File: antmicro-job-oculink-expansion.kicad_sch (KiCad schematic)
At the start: 104 parts, among them J1 OCuLink_x4_Amphenol_G14A42121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, J2 Plug_Samtec_ERM8_2x40_ERM8-04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, U1 MAX3373EEKA+, U2 PI3EQX16904GL, U3 PI3EQX16904GL

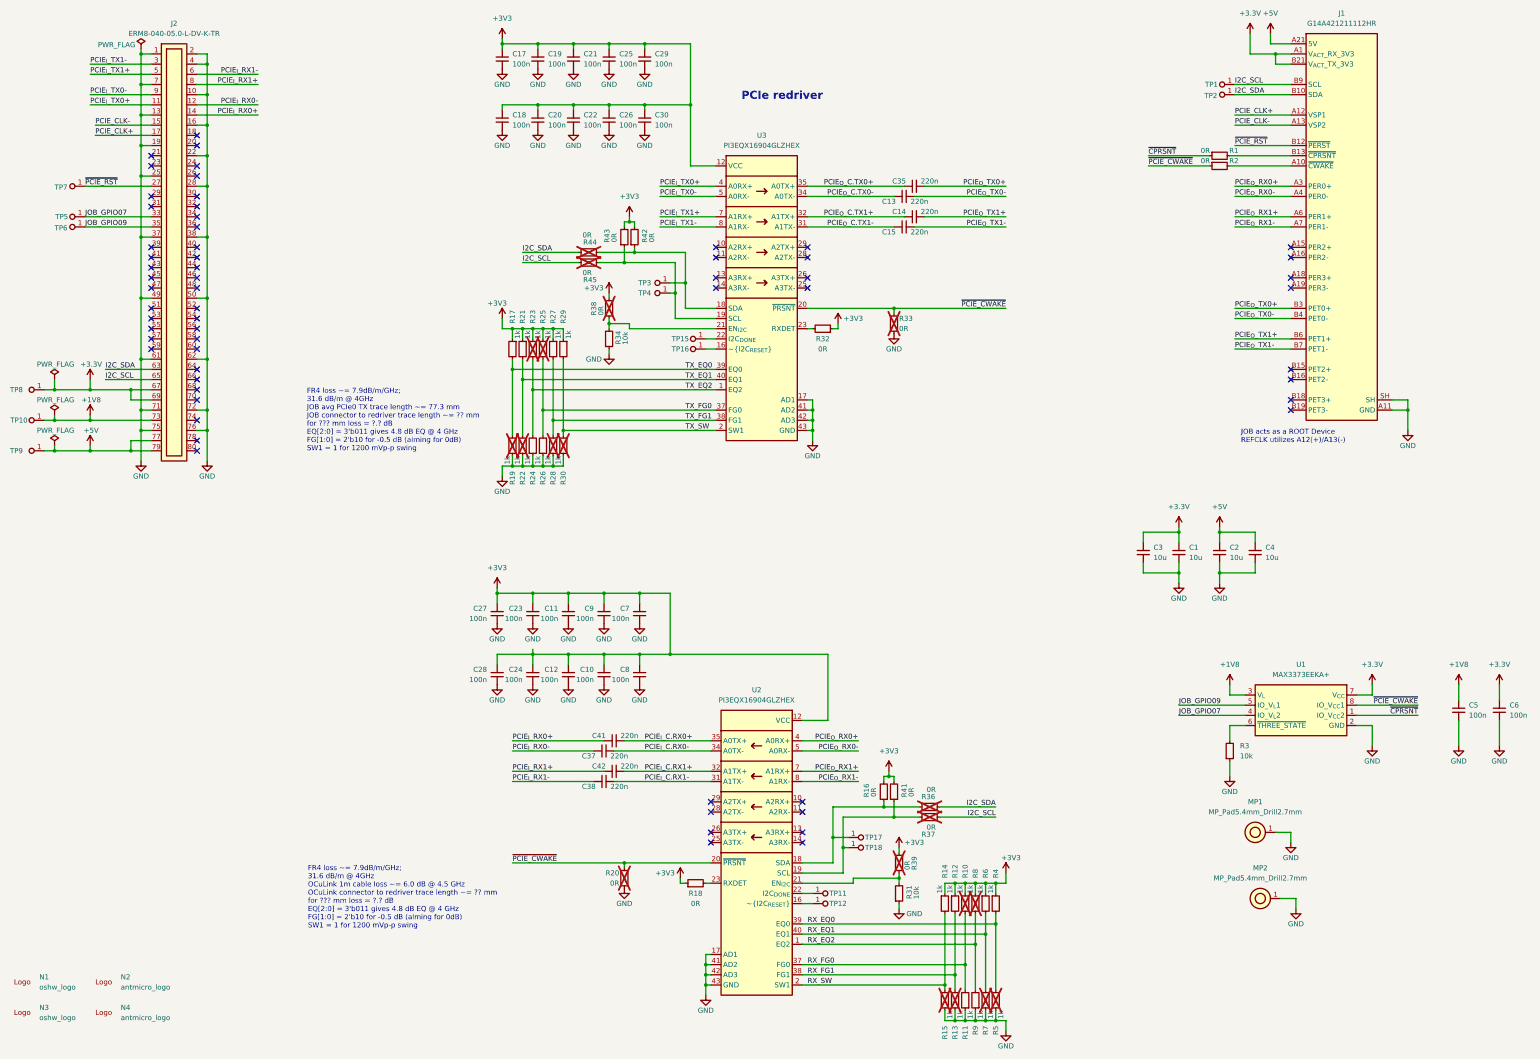
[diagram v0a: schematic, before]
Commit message: [#76297] Rename +3.3V to +3V3
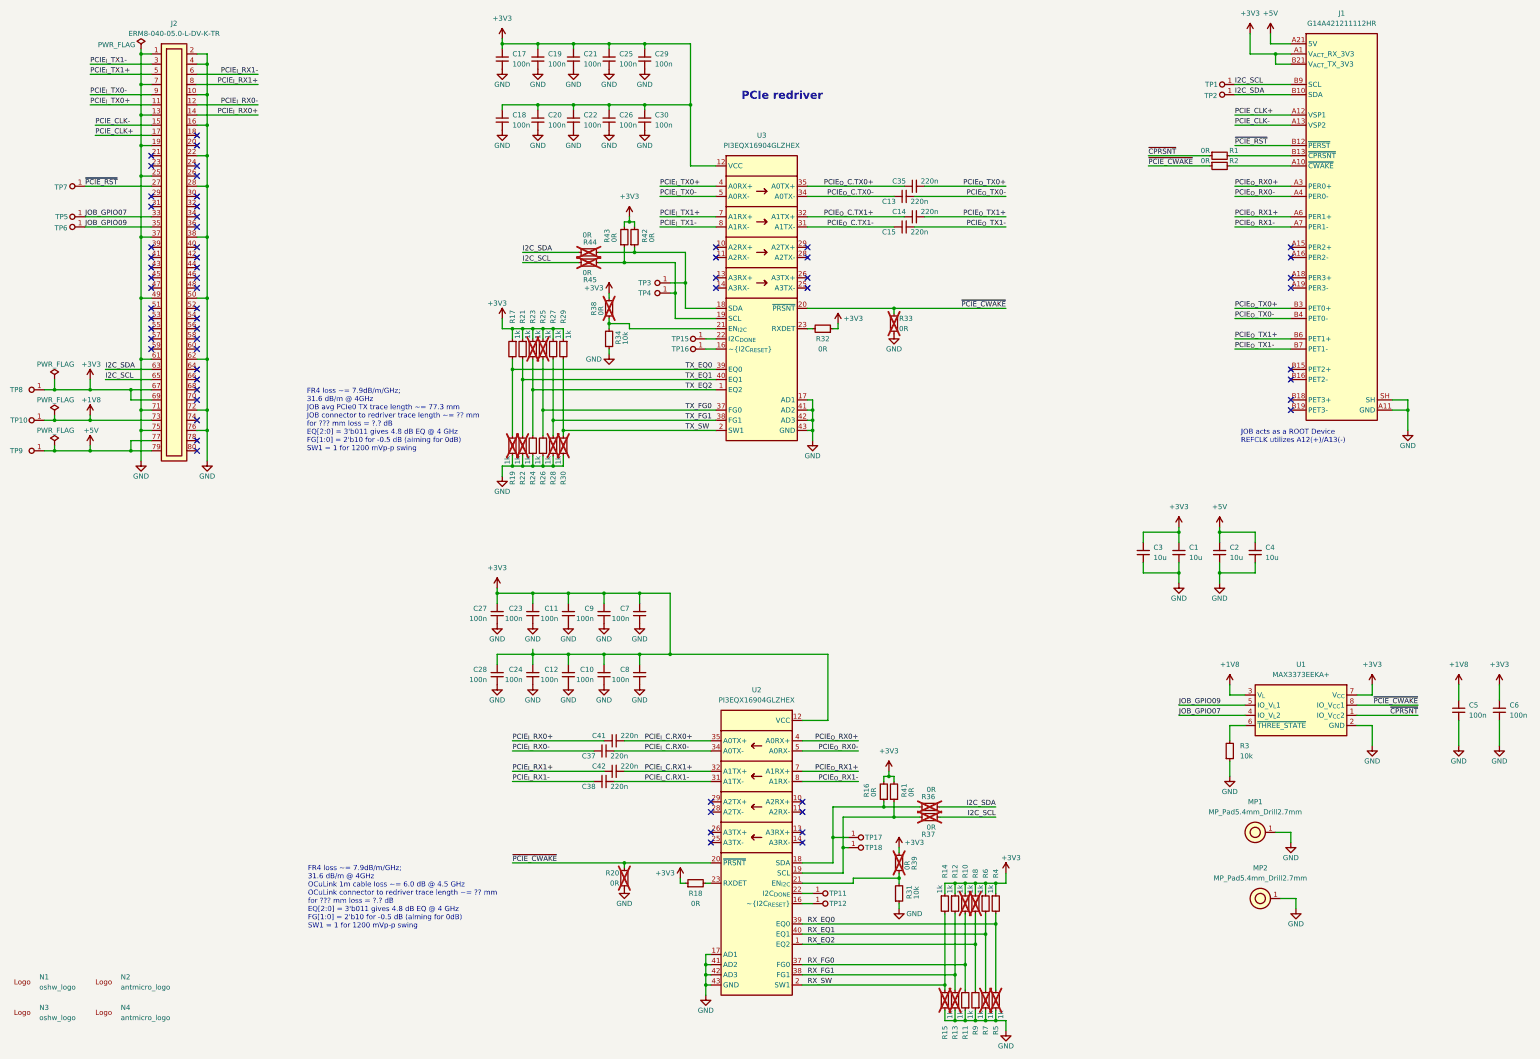
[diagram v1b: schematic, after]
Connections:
- net +3.3V is gone; now on net +3V3: C1.2, C3.2, C6.2, J1.A1 (V_{ACT}_RX_3V3), J1.B21 (V_{ACT}_TX_3V3), J2.67, J2.69, TP8.1, U1.7 (V_{CC})
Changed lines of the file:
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@@
 			)
 		)
-		(property "Value" "+3.3V"
+		(property "Value" "+3V3"
 			(at 396.24 182.88 0)
 			(effects
@@
 			)
 		)
-		(property "Value" "+3.3V"
+		(property "Value" "+3V3"
 			(at 316.23 143.51 0)
 			(effects
@@
 			)
 		)
-		(property "Value" "+3.3V"
+		(property "Value" "+3V3"
 			(at 44.704 107.95 0)
 			(effects
@@
 			)
 		)
-		(property "Value" "+3.3V"
+		(property "Value" "+3V3"
 			(at 334.01 20.32 0)
 			(effects
@@
 			)
 		)
-		(property "Value" "+3.3V"
+		(property "Value" "+3V3"
 			(at 364.49 182.88 0)
 			(effects

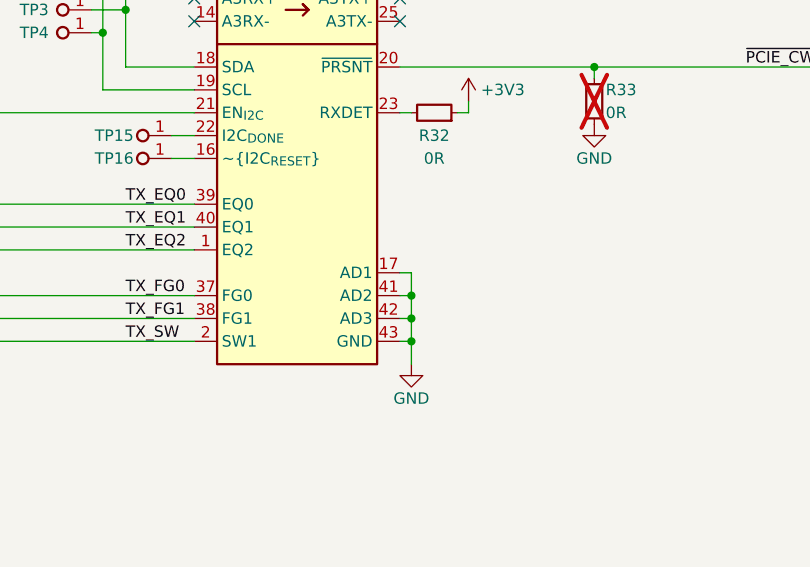
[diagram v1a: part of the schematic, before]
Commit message: [#76297] Fix same redriver I2C addresses
U1 is now accessible on I2C address 0x70 and U2 is accessible on address
0x72.
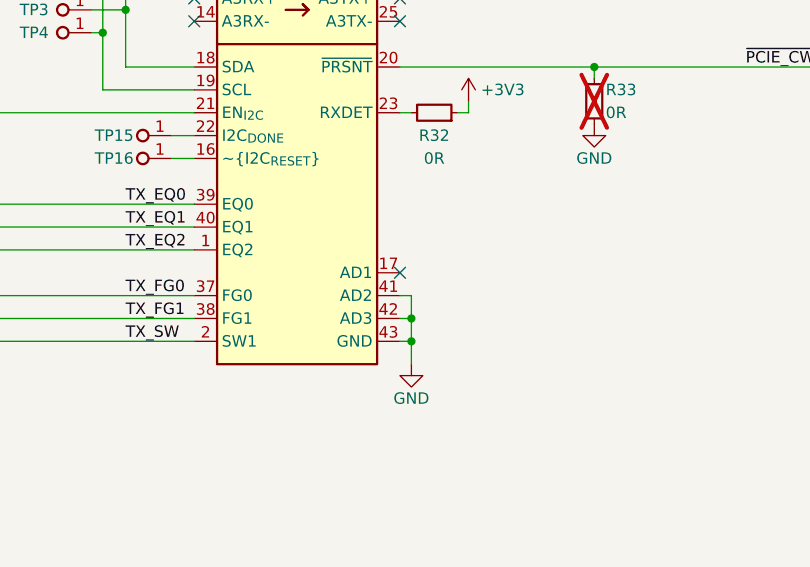
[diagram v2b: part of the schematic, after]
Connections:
- net GND: no longer U3.17 (AD1)
- no-connect marks 63 -> 64
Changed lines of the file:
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@@
-	)
-	(junction
-		(at 224.79 119.38)
-		(diameter 0)
-		(color 0 0 0 0)
 	)
 	(junction
@@
 	)
 	(no_connect
+		(at 223.52 116.84)
+	)
+	(no_connect
 		(at 71.12 104.14)
 	)
@@
 	(wire
 		(pts
-			(xy 224.79 116.84) (xy 224.79 119.38)
-		)
-		(stroke
-			(width 0)
-			(type default)
-		)
-	)
-	(wire
-		(pts
 			(xy 260.35 269.24) (xy 260.35 271.78)
 		)
@@
 		)
 		(stroke
-			(width 0)
-			(type default)
-		)
-	)
-	(wire
-		(pts
-			(xy 223.52 116.84) (xy 224.79 116.84)
-		)
-		(stroke

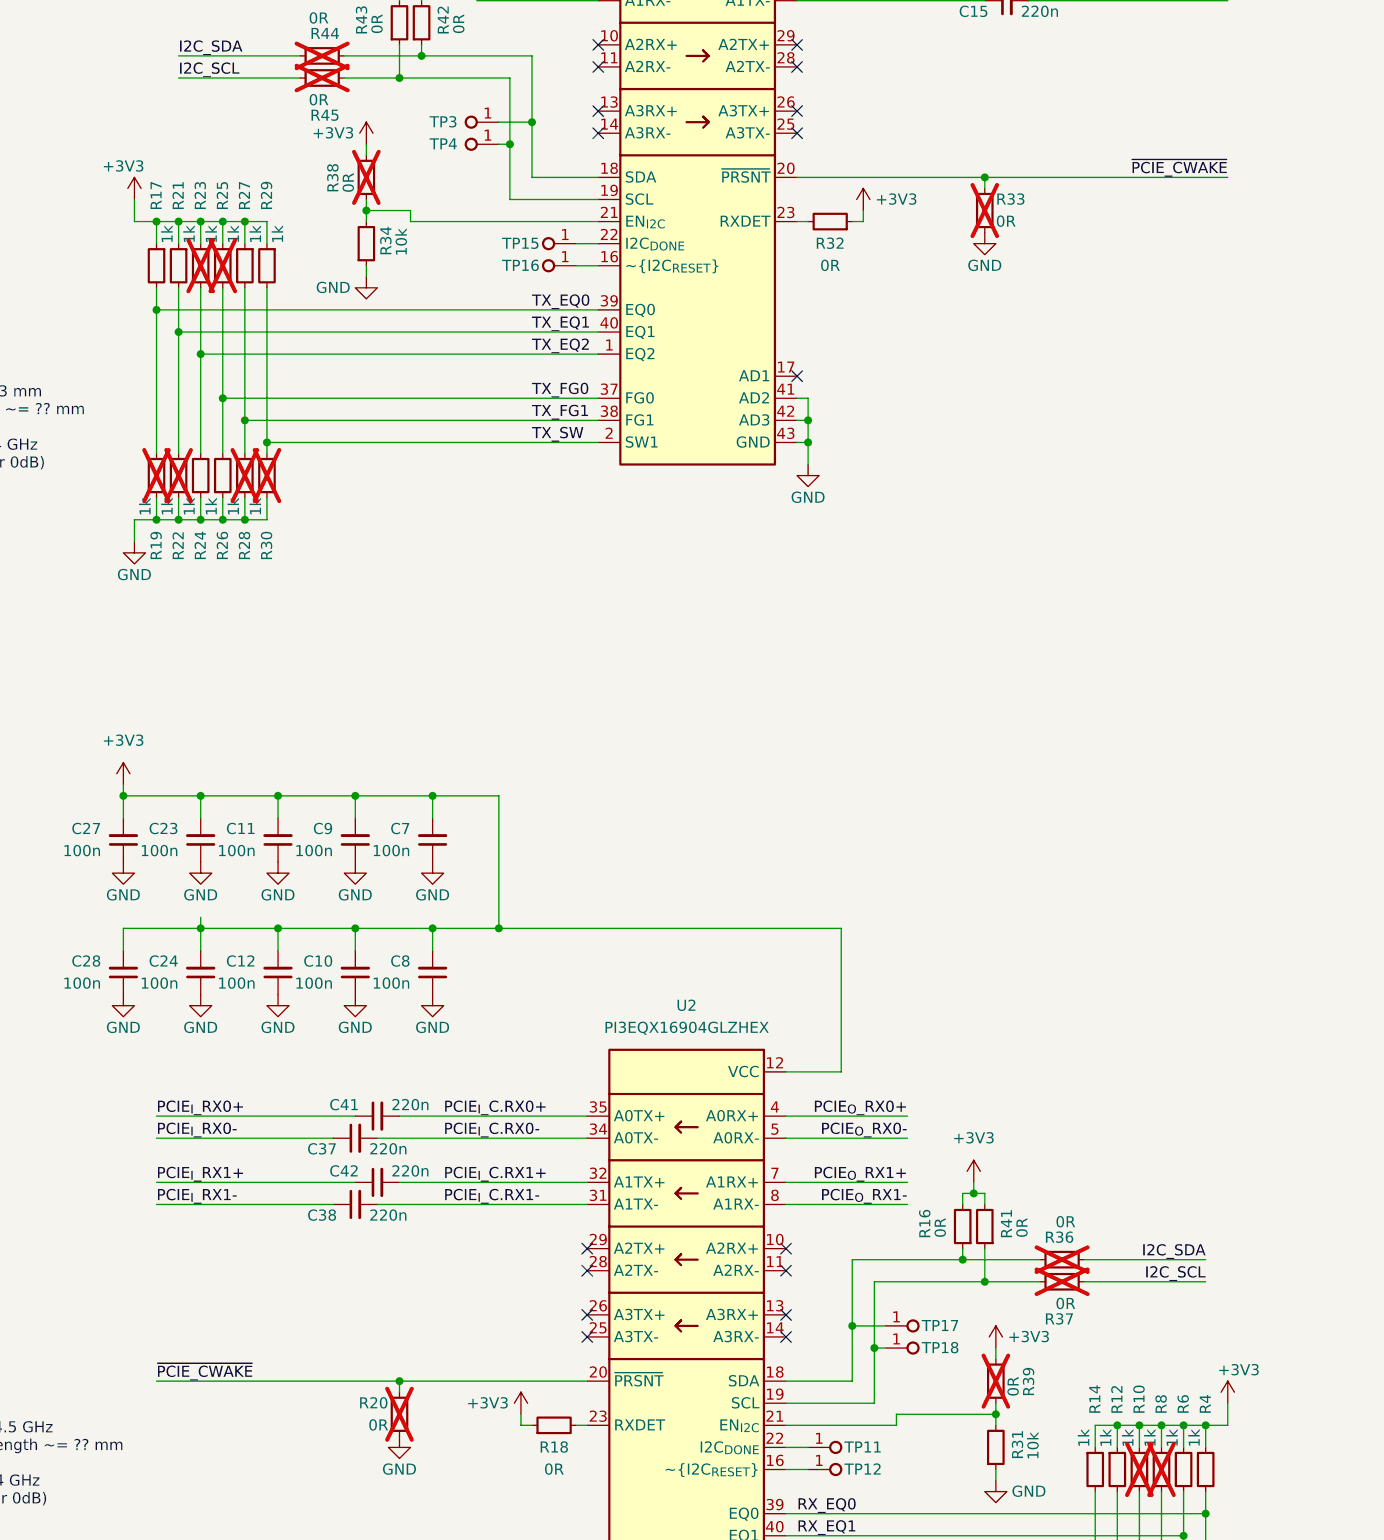
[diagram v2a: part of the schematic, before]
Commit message: [#76297] Connect redriver PRSNT# to CPRSNT#
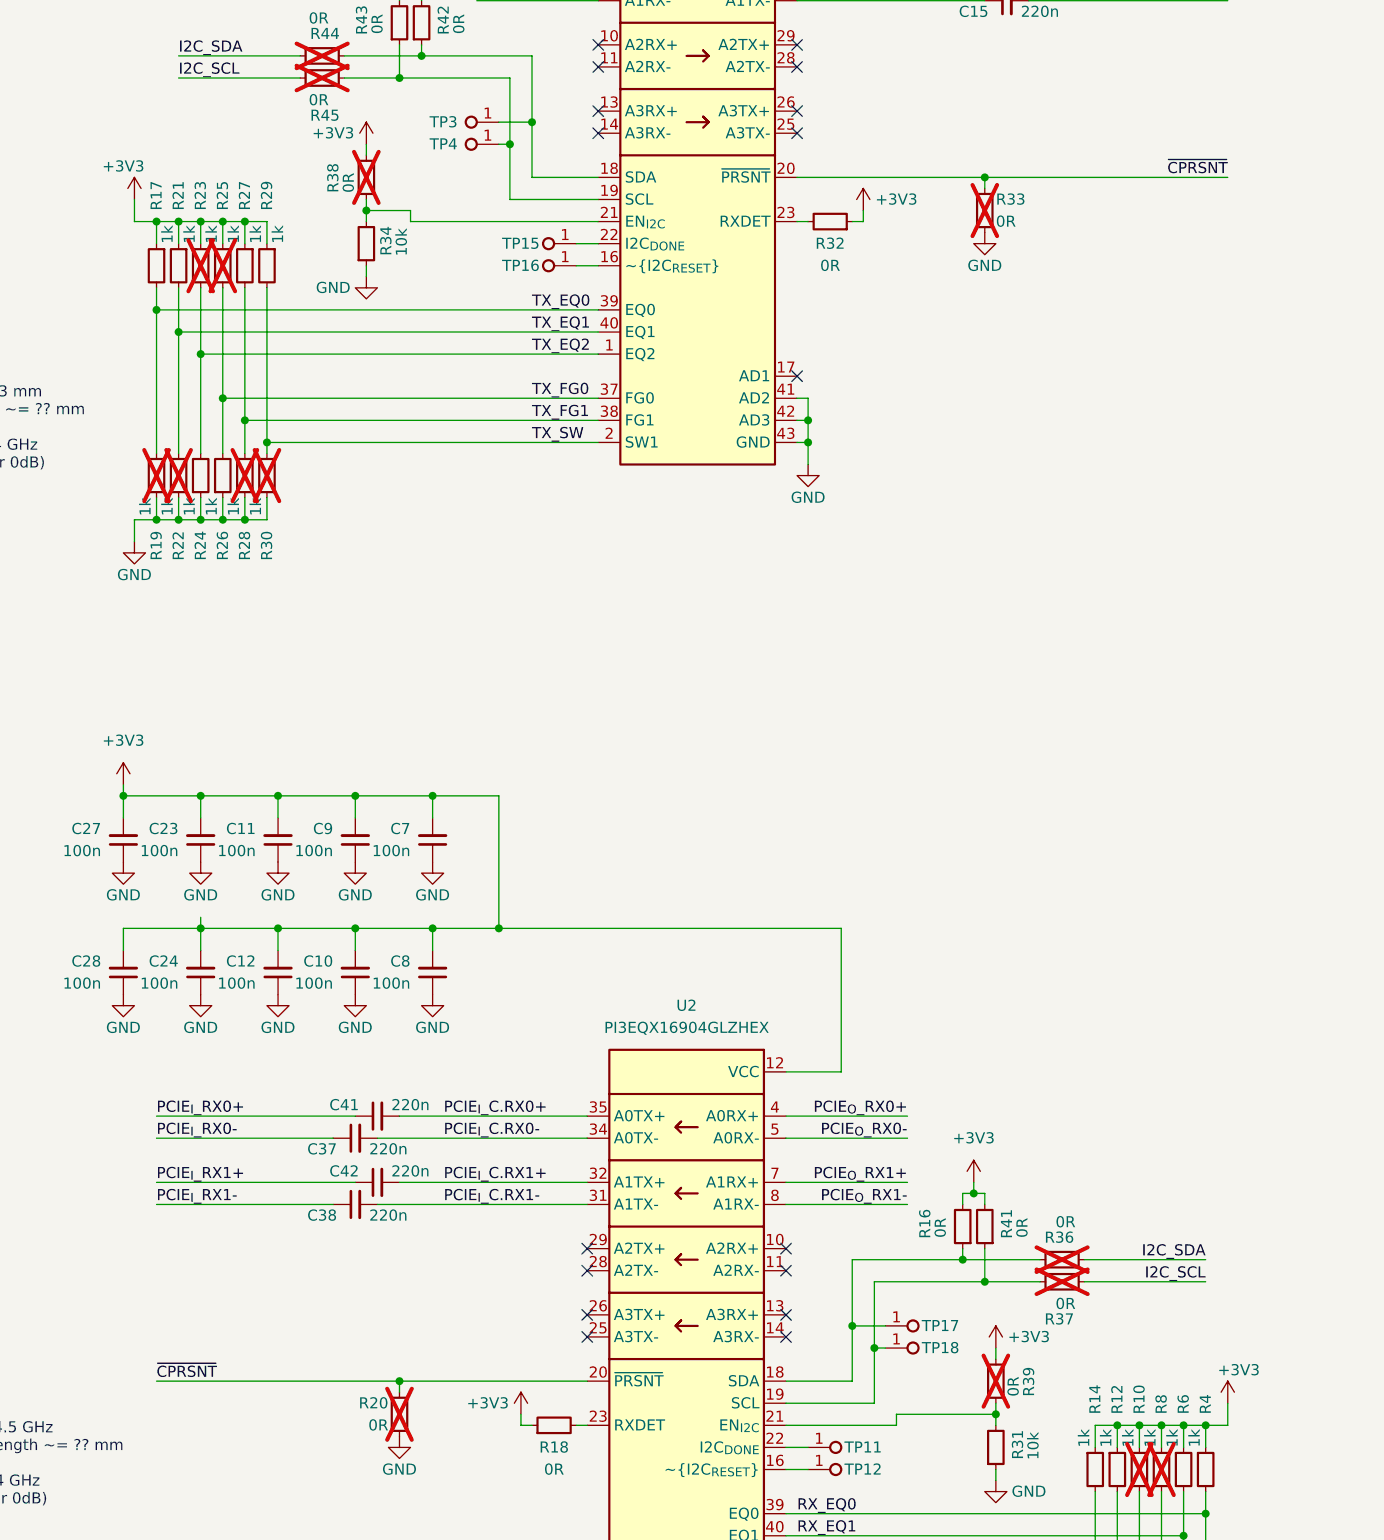
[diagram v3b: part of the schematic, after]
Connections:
- net ~{CPRSNT}: now also R20.2, R33.2, U2.20 (~{PRSNT}), U3.20 (~{PRSNT})
- net ~{PCIE_CWAKE}: no longer R20.2, R33.2, U2.20 (~{PRSNT}), U3.20 (~{PRSNT})
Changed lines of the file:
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@@
 		)
 	)
-	(label "~{PCIE_CWAKE}"
+	(label "~{CPRSNT}"
 		(at 273.05 93.98 180)
 		(fields_autoplaced yes)
@@
 		)
 	)
-	(label "~{PCIE_CWAKE}"
+	(label "~{CPRSNT}"
 		(at 149.86 232.41 0)
 		(fields_autoplaced yes)
